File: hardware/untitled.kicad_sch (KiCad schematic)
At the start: 25 parts, among them Q1 NMOS, Q2 NMOS, U1 LM51231-Q1

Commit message: minor revisions
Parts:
- C8: value ouput cap EEEFK1V471SP 470uf -> EEEFK1V471SP 470uf
- Q1, Q2: value NMOS -> FDMS8820CT-ND
- R1: footprint Resistor_SMD:R_0603_1608Metric -> Resistor_SMD:R_0402_1005Metric
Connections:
- net 21V_CSN: now also C8.1; no longer C8.2
- net GND: now also C8.2; no longer C8.1
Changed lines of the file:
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@@
       (effects (font (size 1.27 1.27)) (justify left))
     )
-    (property "Value" "NMOS" (at 186.8169 100.3227 0)
+    (property "Value" "FDMS8820CT-ND " (at 186.8169 100.3227 0)
       (effects (font (size 1.27 1.27)) (justify left))
     )
@@
     )
   )
-  (symbol (lib_id "Device:C") (at 184.15 82.55 0) (unit 1)
+  (symbol (lib_name "C_1") (lib_id "Device:C") (at 184.15 82.55 0) (unit 1)
     (in_bom yes) (on_board yes) (dnp no) (fields_autoplaced)
     (property "Reference" "C8" (at 187.071 81.9063 0)
       (effects (font (size 1.27 1.27)) (justify left))
     )
-    (property "Value" "ouput cap EEEFK1V471SP 470uf" (at 187.071 83.8273 0)
+    (property "Value" "EEEFK1V471SP 470uf" (at 187.071 83.8273 0)
       (effects (font (size 1.27 1.27)) (justify left))
     )
@@
       (effects (font (size 1.27 1.27)) (justify left))
     )
-    (property "Value" "NMOS" (at 186.8169 116.8327 0)
+    (property "Value" "FDMS8820CT-ND " (at 186.8169 116.8327 0)
       (effects (font (size 1.27 1.27)) (justify left))
     )
@@
       (effects (font (size 1.27 1.27)) (justify left))
     )
-    (property "Footprint" "Resistor_SMD:R_0603_1608Metric" (at 38.862 110.49 90)
-      (effects (font (size 1.27 1.27)) hide)
-    )
+    (property "Footprint" "Resistor_SMD:R_0402_1005Metric" (at 38.862 110.49 90)
+      (effects (font (size 1.27 1.27)) hide)
+    )

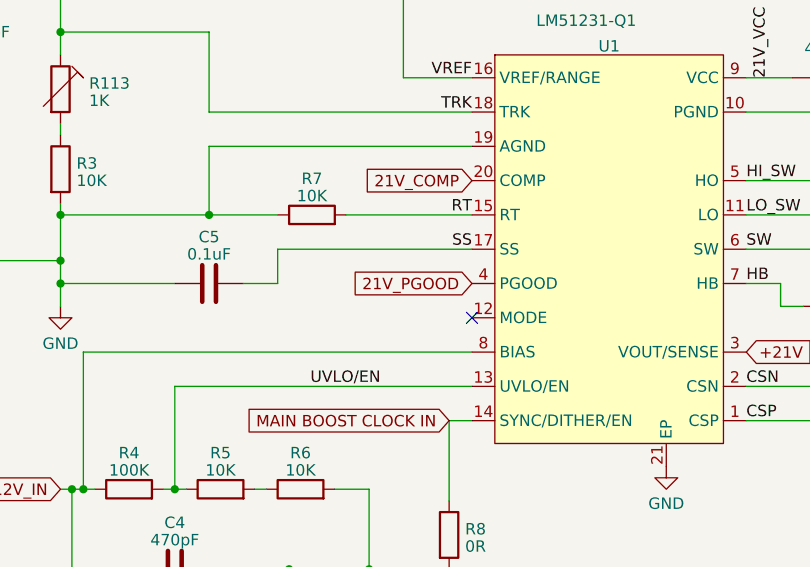
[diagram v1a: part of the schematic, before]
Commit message: switched pd phy as old one needed an NDA
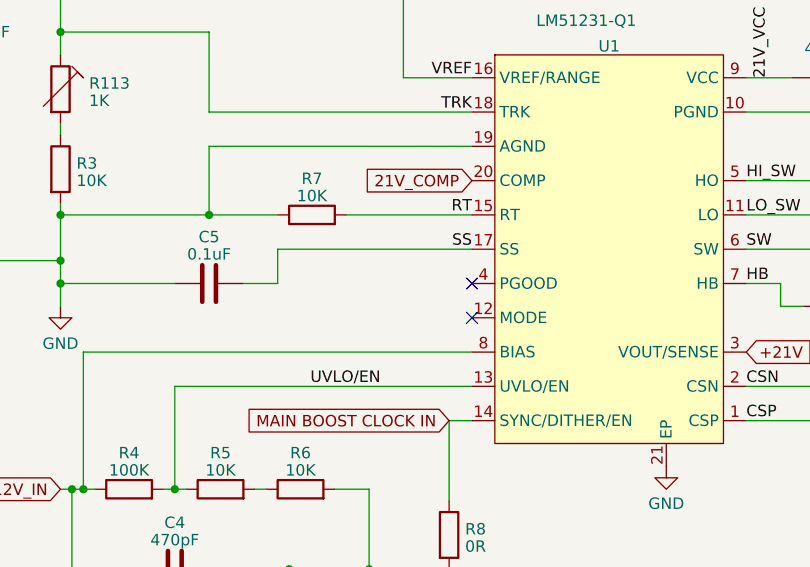
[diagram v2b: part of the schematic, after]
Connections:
- net 21V_PGOOD: no longer names the net of U1.4 (PGOOD)
- no-connect marks 1 -> 2
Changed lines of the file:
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@@
   (junction (at 74.93 69.85) (diameter 0) (color 0 0 0 0)
   )
+  (no_connect (at 120.65 113.03))
   (no_connect (at 120.65 116.84))
   (wire (pts (xy 100.33 144.78) (xy 100.33 146.05))
@@
     )
   )
-  (global_label "21V_PGOOD" (shape input) (at 120.65 113.03 180) (fields_autoplaced)
-    (effects (font (size 1.27 1.27)) (justify right))
-    (property "Intersheetrefs" "${INTERSHEET_REFS}" (at 106.798 113.03 0)
-      (effects (font (size 1.27 1.27)) (justify right) hide)
-    )
-  )

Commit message: switched can tranceiver to combo controler and tranceiver
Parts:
- TP13: footprint TestPoint:TestPoint_Pad_D1.5mm -> TestPoint:TestPoint_Pad_D1.0mm
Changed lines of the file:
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@@
 			)
 		)
-		(property "Footprint" "TestPoint:TestPoint_Pad_D1.5mm"
+		(property "Footprint" "TestPoint:TestPoint_Pad_D1.0mm"
 			(at 204.47 92.71 0)
 			(effects

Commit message: kicad version upgrade and minor pcb changes
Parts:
- added TP46, TP47: TestPoint, TestPoint:TestPoint_Pad_D1.0mm, symbol Connector:TestPoint
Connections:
- net at U1.12 (MODE): now also TP46.1
- net at U1.4 (PGOOD): now also TP47.1
- no-connect marks 2 -> 0
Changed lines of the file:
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@@
 		(color 0 0 0 0)
 	)
-	(no_connect
-		(at 120.65 113.03)
-	)
-	(no_connect
-		(at 120.65 116.84)
-	)
 	(wire
 		(pts
@@
 	(wire
 		(pts
+			(xy 118.11 113.03) (xy 118.11 115.57)
+		)
+		(stroke
+			(width 0)
+			(type default)
+		)
+	)
+	(wire
+		(pts
 			(xy 40.64 104.14) (xy 40.64 106.68)
 		)
@@
 	(wire
 		(pts
+			(xy 120.65 116.84) (xy 120.65 118.11)
+		)
+		(stroke
+			(width 0)
+			(type default)
+		)
+	)
+	(wire
+		(pts
 			(xy 172.72 124.46) (xy 151.13 124.46)
 		)
@@
 	(wire
 		(pts
+			(xy 120.65 118.11) (xy 105.41 118.11)
+		)
+		(stroke
+			(width 0)
+			(type default)
+		)
+	)
+	(wire
+		(pts
 			(xy 52.07 128.27) (xy 45.72 128.27)
 		)
@@
 	(wire
 		(pts
+			(xy 118.11 115.57) (xy 113.03 115.57)
+		)
+		(stroke
+			(width 0)
+			(type default)
+		)
+	)
+	(wire
+		(pts
 			(xy 163.83 90.17) (xy 166.37 90.17)
 		)
@@
 		(pts
 			(xy 113.03 90.17) (xy 120.65 90.17)
+		)
+		(stroke
+			(width 0)
+			(type default)
+		)
+	)
+	(wire
+		(pts
+			(xy 120.65 113.03) (xy 118.11 113.03)
 		)
 		(stroke
@@
 	)
 	(symbol
+		(lib_id "Connector:TestPoint")
+		(at 105.41 118.11 90)
+		(unit 1)
+		(exclude_from_sim no)
+		(in_bom yes)
+		(on_board yes)
+		(dnp no)
+		(fields_autoplaced yes)
+		(property "Reference" "TP46"
+			(at 102.108 113.3305 90)
+			(effects
+				(font
+					(size 1.27 1.27)
+				)
+			)
+		)
+		(property "Value" "TestPoint"
+			(at 102.108 115.7548 90)
+			(effects
+				(font
+					(size 1.27 1.27)
+				)
+			)
+		)
+		(property "Footprint" "TestPoint:TestPoint_Pad_D1.0mm"
+			(at 105.41 113.03 0)
+			(effects
+				(font
+					(size 1.27 1.27)
+				)
+				(hide yes)
+			)
+		)
+		(property "Datasheet" "~"
+			(at 105.41 113.03 0)
+			(effects
+				(font
+					(size 1.27 1.27)
+				)
+				(hide yes)
+			)
+		)
+		(property "Description" ""
+			(at 105.41 118.11 0)
+			(effects
+				(font
+					(size 1.27 1.27)
+				)
+				(hide yes)
+			)
+		)
+		(pin "1"
+		)
+		(instances
+			(project "usbc-car-module"
+				(path "/fae025e9-99c5-40c1-af6f-99dc1edbfa43/d2e16279-165c-4434-90cd-263b76553257"
+					(reference "TP46")
+					(unit 1)
+				)
+			)
+		)
+	)
+	(symbol
 		(lib_name "NMOS_1")
 		(lib_id "Simulation_SPICE:NMOS")
@@
 					(unit 1)
 				)
+			)
+		)
+	)
+	(symbol
+		(lib_id "Connector:TestPoint")
+		(at 113.03 115.57 90)
+		(unit 1)
+		(exclude_from_sim no)
+		(in_bom yes)
+		(on_board yes)
+		(dnp no)
+		(fields_autoplaced yes)
+		(property "Reference" "TP47"
+			(at 109.728 110.7905 90)
+			(effects
+				(font
+					(size 1.27 1.27)
+				)
+			)
+		)
+		(property "Value" "TestPoint"
+			(at 109.728 113.2148 90)
+			(effects
+				(font
+					(size 1.27 1.27)
+				)
+			)
+		)
+		(property "Footprint" "TestPoint:TestPoint_Pad_D1.0mm"
+			(at 113.03 110.49 0)
+			(effects
+				(font
+					(size 1.27 1.27)
+				)
+				(hide yes)
+			)
+		)
+		(property "Datasheet" "~"
+			(at 113.03 110.49 0)
+			(effects
+				(font
+					(size 1.27 1.27)
+				)
+				(hide yes)
+			)
+		)
+		(property "Description" ""
+			(at 113.03 115.57 0)
+			(effects
+				(font
+					(size 1.27 1.27)
+				)
+				(hide yes)
+			)
+		)
+		(pin "1"
+		)
+		(instances
+			(project "usbc-car-module"
+				(path "/fae025e9-99c5-40c1-af6f-99dc1edbfa43/d2e16279-165c-4434-90cd-263b76553257"
+					(reference "TP47")
+					(unit 1)
+				)

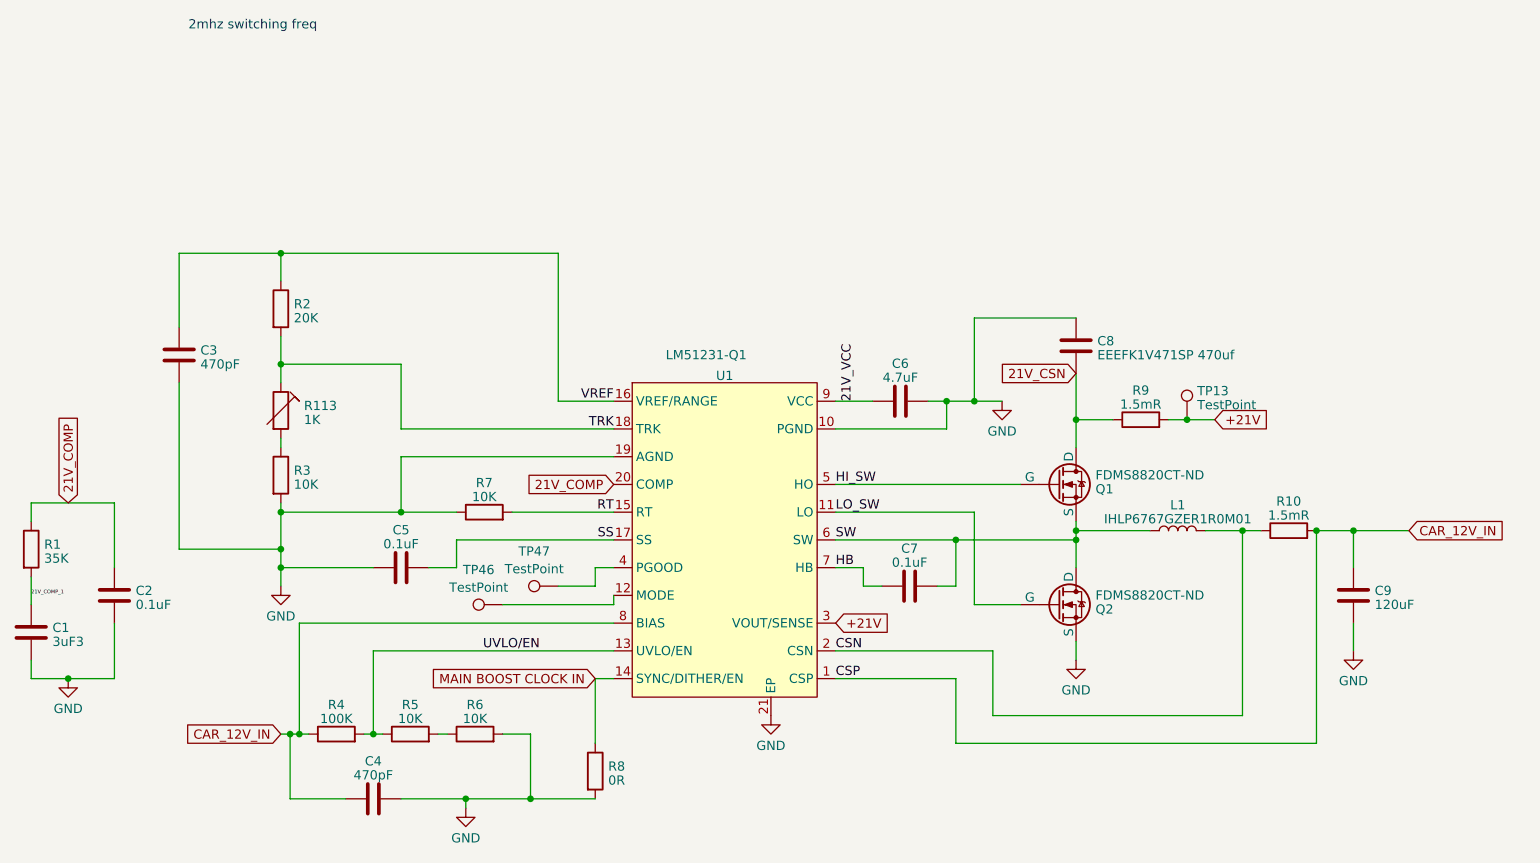
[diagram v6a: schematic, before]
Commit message: migrated to the esp32-s2 and starting new board revison
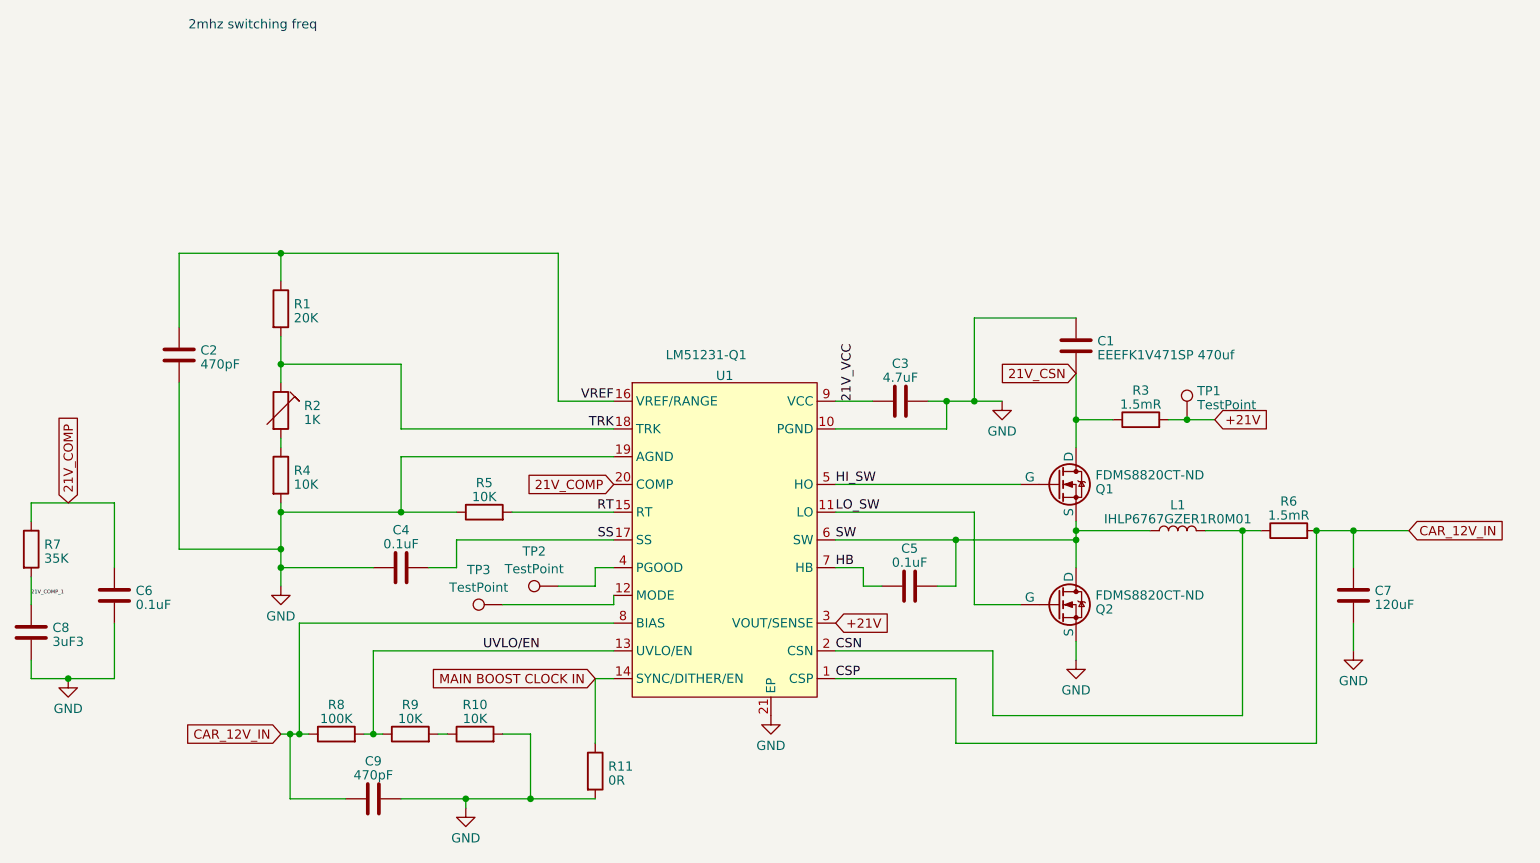
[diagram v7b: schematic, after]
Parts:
- Q1, Q2: value FDMS8820CT-ND -> FDMS8820CT-ND
- R7: renamed from R1; footprint Resistor_SMD:R_0402_1005Metric -> Resistor_SMD:R_0603_1608Metric
- U1: footprint PCM_Package_DFN_QFN_AKL:QFN-20-1EP_3.5x3.5mm_P0.5mm_EP2x2mm_ThermalVias -> Package_DFN_QFN:QFN-20-1EP_3.5x3.5mm_P0.5mm_EP2x2mm_ThermalVias
- renumbered C8 to C1, C3 to C2, C6 to C3, C5 to C4, C7 to C5, C2 to C6, C9 to C7, C1 to C8, C4 to C9, R2 to R1, R6 to R10, R8 to R11, R113 to R2, R9 to R3, R3 to R4, R7 to R5, R10 to R6, R4 to R8, R5 to R9, TP13 to TP1, TP47 to TP2, TP46 to TP3
